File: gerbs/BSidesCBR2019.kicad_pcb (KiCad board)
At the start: 2 copper layers, 44.9 x 114.1 mm, 38 parts, among them IC1 Si4455-B1A-FM, J1 SAO, J2 LSAO, SW1 RESET, U1 ATMEGA328P-AU, U2 Nokia_5110_LCD, Y1 16Mhz, Y2 30Mhz

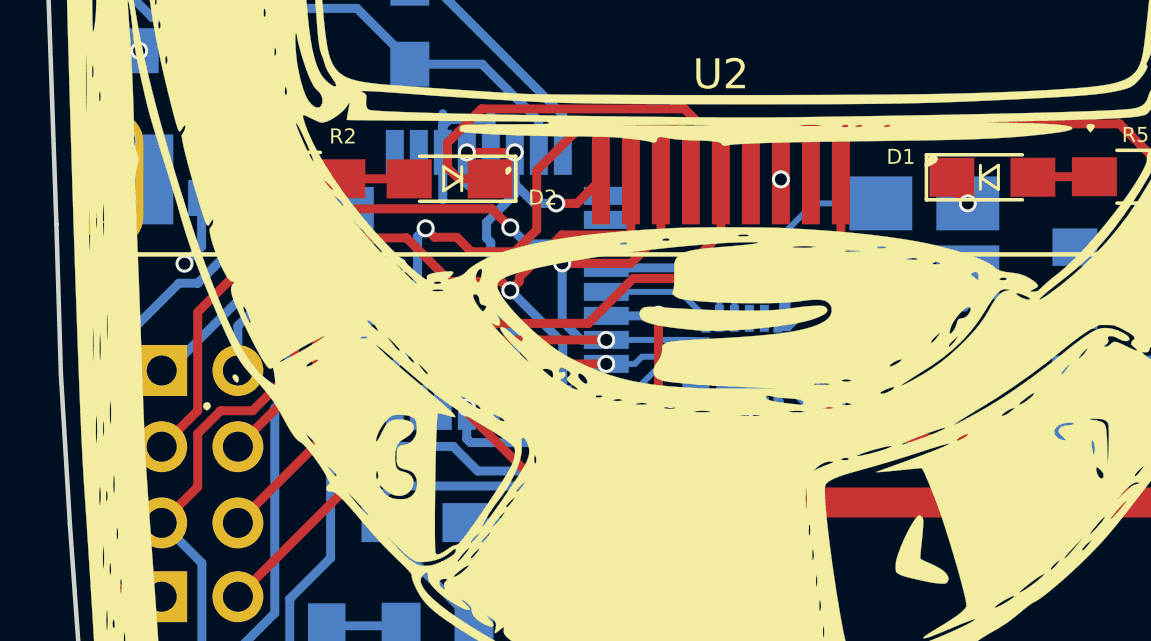
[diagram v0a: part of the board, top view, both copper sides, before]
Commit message: Regen gerbers and update footprint for si4455
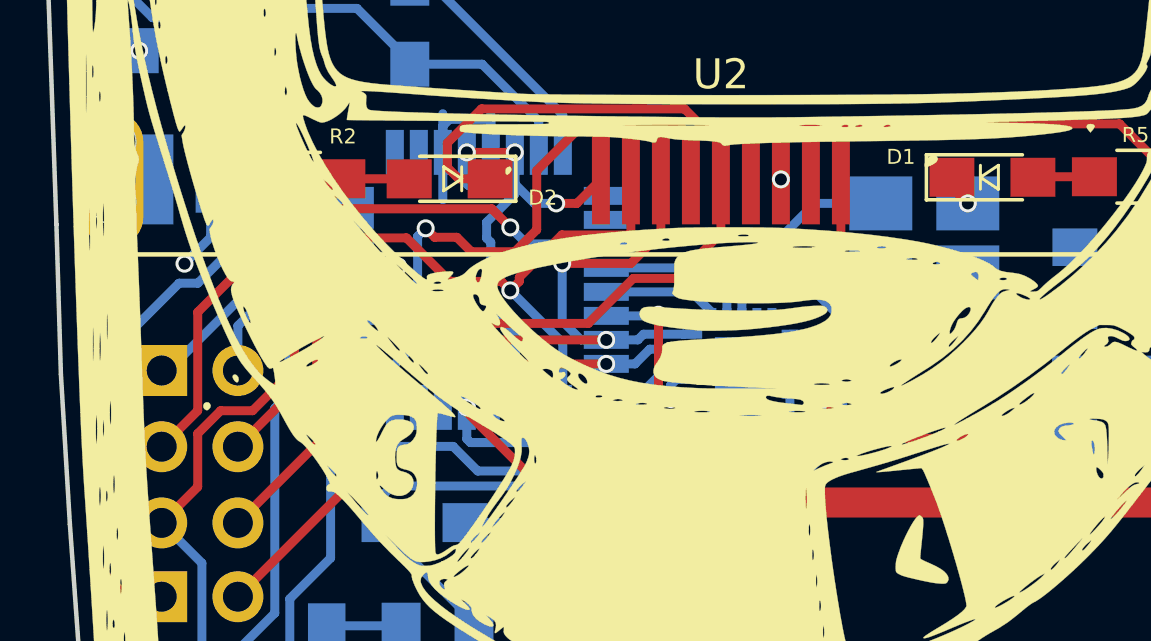
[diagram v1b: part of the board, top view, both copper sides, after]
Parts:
- D5: footprint Diodes_SMD:D_SOD-123 -> Diodes_SMD:D_SOD-323_HandSoldering
- IC1: footprint Silicon Labs - Si4455-B1A-FM:SILICON_LABS_SI4455-B1A-FM_0 -> Si4455-B1A-FM:QFN50P300X300X80-21N-D
- moved D5 0.10 mm to (43.3, 103.2)
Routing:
- net +3.3v: track 27.0 -> 34.3 mm, vias 14 -> 13
- net GND: track 39.5 -> 36.5 mm
- net /XIN: track 11.1 -> 9.84 mm
- net /TXA: track 32.4 -> 31.7 mm
- net RESET: track 80.8 -> 80.3 mm
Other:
- net class Thinz removed
